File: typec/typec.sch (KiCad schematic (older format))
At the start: 26 parts, among them U1 TPD6E05U06-USON, U2 TPD4E05U06-USON, U3 TPS62081-WSON, U4 TPD4E05U06-USON, U5 TPS74801-VSON, U6 TUSB212-X2QFN

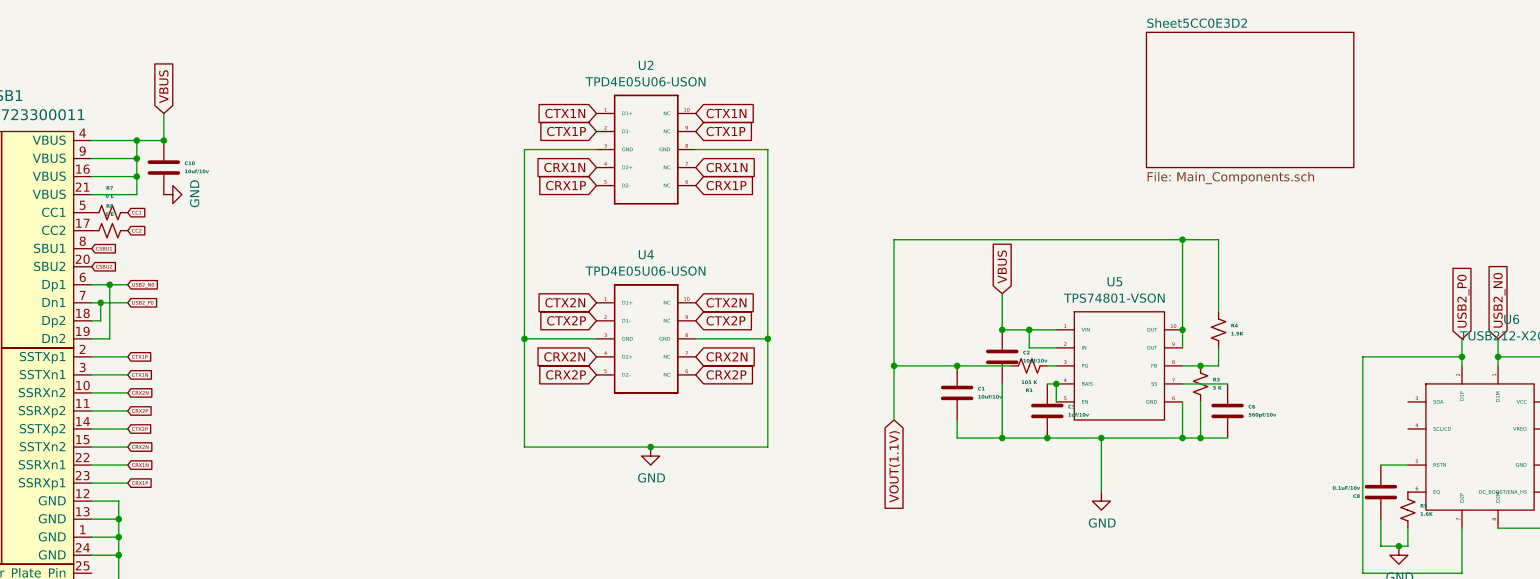
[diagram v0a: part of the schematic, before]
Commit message: Added another page and completed the Multiplexer schematics.
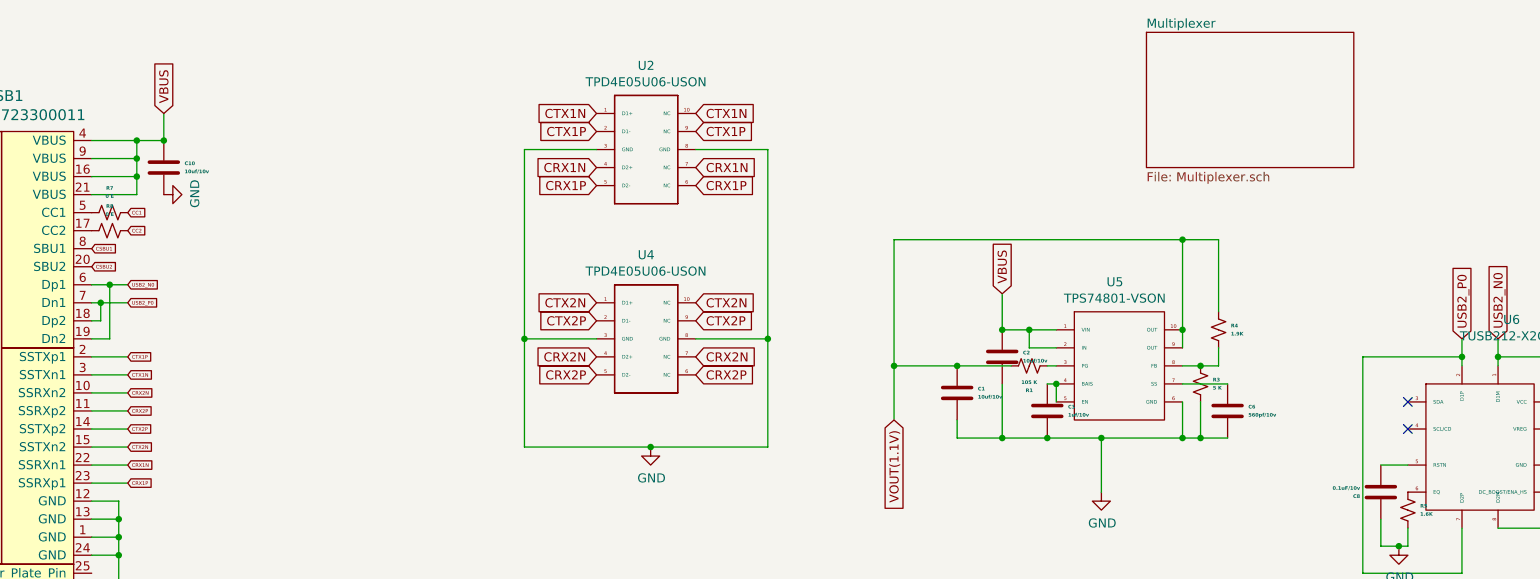
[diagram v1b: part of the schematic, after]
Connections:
- net CRX2N: no longer USB1.15 (SSTXn2)
- net CTX2N: now also USB1.15 (SSTXn2)
- no-connect marks 0 -> 2
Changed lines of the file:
@@
 $Descr A4 11693 8268
 encoding utf-8
-Sheet 1 2
+Sheet 1 3
 Title ""
 Date ""
@@
 	2750 3650 2550 3650
 Text GLabel 2750 3750 2    20   Input ~ 0
-CRX2N
+CTX2N
 Wire Wire Line
 	2750 3750 2550 3750
@@
 S 8400 1450 1150 750
 U 5CC0E3D3
-F0 "Sheet5CC0E3D2" 50
-F1 "Main_Components.sch" 50
+F0 "Multiplexer" 50
+F1 "Multiplexer.sch" 50
 $EndSheet
+NoConn ~ 9850 3500
+NoConn ~ 9850 3650
 $EndSCHEMATC

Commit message: updated
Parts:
- removed C1: 10uf/10v, Capacitor_SMD:C_0805_2012Metric, symbol Device:C
- removed C9: 0.1uF/10v, Capacitor_SMD:C_0402_1005Metric, symbol Device:C
- removed U3: TPS62081-WSON, TPS62081-WSON:TPS62081-WSON, symbol typec-rescue:TPS62081-WSON-TPS62081-WSON
- removed U5: TPS74801-VSON, TPS74801-VSON:TPS74801-VSON, symbol typec-rescue:TPS74801-VSON-TPS74801-VSON
- removed U6: TUSB212-X2QFN, TUSB212-X2QFN:TUSB212-X2QFN, symbol TUSB212-X2QFN:TUSB212-X2QFN
- added D1, D2, D3, D4, D5: LED, LED_SMD:LED_0402_1005Metric, symbol Device:LED
- added JP1, JP2: Jumper_NO_Small, Connector_PinHeader_1.00mm:PinHeader_1x02_P1.00mm_Vertical, symbol Device:Jumper_NO_Small
- added R10: 1.9K, Resistor_SMD:R_0402_1005Metric, symbol Device:R_Small_US
- added R9: 330 E, Resistor_SMD:R_0402_1005Metric, symbol Device:R_Small_US
- added SW1: SW_Push_Dual_x2, Button_Switch_THT:SW_DIP_SPSTx01_Slide_6.7x4.1mm_W7.62mm_P2.54mm_LowProfile, symbol Switch:SW_Push_Dual_x2
- added TP1, TP2: TestPoint, TestPoint:TestPoint_THTPad_2.0x2.0mm_Drill1.0mm, symbol Connector:TestPoint
- added U2: TUSB212-X2QFN, TUSB212-X2QFN:TUSB212-X2QFN, symbol TUSB212-X2QFN:TUSB212-X2QFN
- added U5: TPS62082-WSON, TPS62081-WSON:TPS62082-WSON, symbol typec-rescue:TPS62082-WSON
- added U6: TPS74801-VSON, TPS74801-VSON:TPS74801-VSON, symbol TPS74801-VSON:TPS74801-VSON
- added e1: 105 K, Resistor_SMD:R_0201_0603Metric, symbol Device:R_Small_US
- C2: value 10uf/10v -> 0.1uF/10v; footprint Capacitor_SMD:C_0805_2012Metric -> Capacitor_SMD:C_0402_1005Metric
- C3: value 1uf/10v -> 10uf/10v
- C4: value 10 uF/10V -> 1uf/10v; footprint Capacitor_SMD:C_0805_2012Metric -> Capacitor_SMD:C_0603_1608Metric
- C5: value 22uf/6.3v -> 10 uF/10V; footprint Capacitor_SMD:C_0805_2012Metric -> Capacitor_SMD:C_0603_1608Metric
- C6: value 560pf/10v -> 590pf/10v; footprint Capacitor_SMD:C_0402_1005Metric -> Capacitor_SMD:C_0201_0603Metric
- C7: value 10uf/10v -> 22uf/6.3v; footprint Capacitor_SMD:C_0805_2012Metric -> Capacitor_SMD:C_0603_1608Metric
- C8: value 0.1uF/10v -> 10uf/10v; footprint Capacitor_SMD:C_0402_1005Metric -> Capacitor_SMD:C_0603_1608Metric
- R1: value 105 K -> 1.6K; footprint Resistor_SMD:R_0805_2012Metric -> Resistor_SMD:R_0201_0603Metric
- R2: value 178K -> 330 E; footprint Resistor_SMD:R_0805_2012Metric -> Resistor_SMD:R_0402_1005Metric
- R3: value 5 K -> 330 E; footprint Resistor_SMD:R_0805_2012Metric -> Resistor_SMD:R_0201_0603Metric
- R4: value 1.9K -> 43K; footprint Resistor_SMD:R_0805_2012Metric -> Resistor_SMD:R_0201_0603Metric
- R5: value 1.6K -> 100 E; footprint Resistor_SMD:R_0805_2012Metric -> Resistor_SMD:R_0402_1005Metric
- R6: value 43K -> 330 E; footprint Resistor_SMD:R_0805_2012Metric -> Resistor_SMD:R_0402_1005Metric
- R7: value 0 E -> 178K; footprint Resistor_SMD:R_0805_2012Metric -> Resistor_SMD:R_0402_1005Metric
- R8: value 0 E -> 5 K; footprint Resistor_SMD:R_0805_2012Metric -> Resistor_SMD:R_0402_1005Metric
- renumbered C10 to C1, U2 to U3
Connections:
- net CC1: now also USB1.5 (CC1); no longer R7.1, U1.14 (D+)
- net CC2: now also U1.6 (NC), USB1.17 (CC2); no longer R8.1, U1.13 (D-), U1.2 (NC)
- net CRX1N: now also U3.1 (D1+); no longer U3.4 (D2+), U3.7 (NC)
- net CRX1P: now also U3.2 (D1-); no longer U3.5 (D2-), U3.6 (NC)
- net CRX2N: now also U4.1 (D1+); no longer U4.4 (D2+), U4.7 (NC)
- net CRX2P: now also U4.2 (D1-); no longer U4.5 (D2-), U4.6 (NC)
- net CSBU1: no longer U1.8 (D3-)
- net CSBU2: now also U1.2 (NC); no longer U1.6 (NC), U1.9 (D3+)
- net CTX1N: now also U3.5 (D2-); no longer U3.1 (D1+), U3.10 (NC)
- net CTX1P: now also U3.4 (D2+); no longer U3.2 (D1-), U3.9 (NC)
- net CTX2N: now also U4.5 (D2-); no longer U4.1 (D1+), U4.10 (NC)
- net CTX2P: now also U4.4 (D2+); no longer U4.2 (D1-), U4.9 (NC)
- net GND: now also C8.2, R1.2, R8.1, USB1.25 (Center_Plate_Pin), USB1.26 (Connector_Legs), USB1.27 (Under-Barrel_Pads), D1.1 (K), D2.1 (K), D3.1 (K), D4.1 (K), D5.1 (K), JP1.1, JP2.1, SW1.1 (C), U2.10 (GND), U5.2 (GND), U5.3 (MODE), U5.4 (FB), U5.9 (GND), U6.11 (GND), U6.6 (GND); no longer C8.1, R3.1, R5.2
- net USB2_N0: now also U2.1 (D1M); no longer U1.3 (NC), USB1.19 (Dn2), USB1.6 (Dp1)
- net USB2_P0: now also U2.2 (D1P); no longer U1.4 (NC), USB1.18 (Dp2), USB1.7 (Dn1)
- net VBUS: now also C5.1, R2.1, TP1.1, U5.1 (EN), U5.8 (VIN); no longer C2.1, C4.1
- net VOUT(1.1V): now also C3.1, R10.1, U6.10 (OUT), U6.9 (OUT), e1.2; no longer R1.1, R4.1
- net VOUT(3.3V): now also C4.1, C8.1, R3.1, R4.1, R7.2, R9.1, TP2.1, U2.12 (VCC), U5.5 (VOS), U6.1 (VIN), U6.2 (IN), U6.4 (BAIS), U6.5 (EN); no longer C5.1, R2.2
- net at L1.1: now also U5.7 (SW)
- net at C6.1: now also U6.7 (SS)
- net at R3.2: now also D2.2 (A); no longer R4.2
- net SCL: now reaches R5.1
- net SCL: now also JP2.2, U2.4 (SCL/CD)
- net at R6.2: now also D4.2 (A)
- net at R8.2: now also R10.2, U6.8 (FB); no longer USB1.17 (CC2)
- new net: U6.3 (PG), e1.1
- new net: SW1.2 (D), U2.5 (RSTN)
- new net: JP1.2, U2.3 (SDA)
- new net: R1.1, U2.6 (EQ)
- new net: R4.2, U2.9 (DC_BOOST/ENA_HS)
- new net: C2.1, U2.11 (VREG)
- new net: D3.2 (A), R5.2
- new net: R7.1, U5.6 (PG)
- new net: D5.2 (A), R9.2
- new net: D1.2 (A), R2.2
- new net CC10: U1.14 (D+)
- new net CC20: U1.9 (D3+)
- new net CRX1N0: U3.10 (NC)
- new net CRX1P0: U3.9 (NC)
- new net CRX2N0: U4.10 (NC)
- new net CRX2P0: U4.9 (NC)
- new net CSBU10: U1.8 (D3-)
- new net CSBU20: U1.13 (D-)
- new net CTX1N0: U3.6 (NC)
- new net CTX1P0: U3.7 (NC)
- new net CTX2N0: U4.6 (NC)
- new net CTX2P0: U4.7 (NC)
- new net USB2_N: U1.3 (NC), USB1.19 (Dn2), USB1.6 (Dp1)
- new net USB2_N10: U2.8 (D2M)
- new net USB2_P: U1.4 (NC), USB1.18 (Dp2), USB1.7 (Dn1)
- new net USB2_P10: U2.7 (D2P)
- no-connect marks 2 -> 0
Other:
- moved on the sheet: U1, U3, U4

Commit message: 2.0
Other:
- moved on the sheet: C5, C7, C8, D5, L1, R7, R9, TP1, TP2, U5
